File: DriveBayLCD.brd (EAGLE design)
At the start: 57.4 x 41.3 mm, 31 parts, among them J1 AVR_SPI_PRG_6PTH, U1 ATMEGA32U2-AU, U2 2N7002, X1 22-23-2041

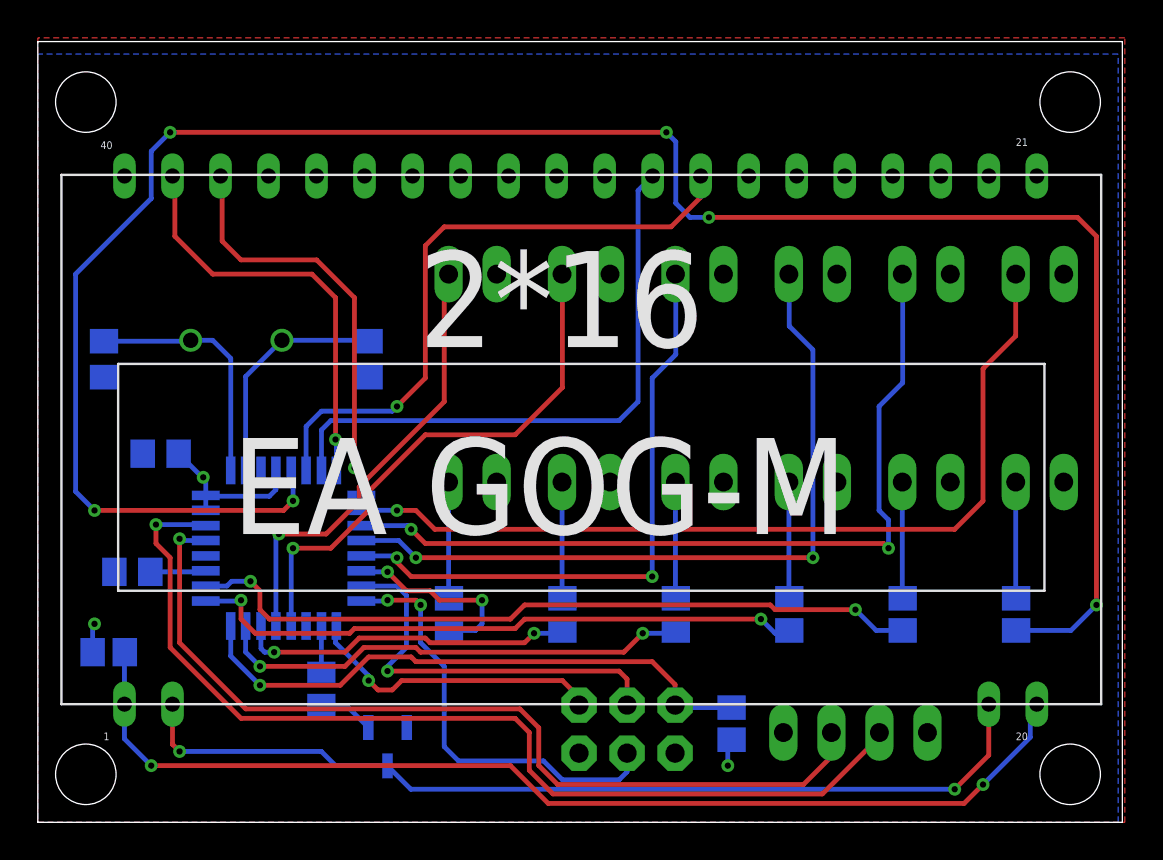
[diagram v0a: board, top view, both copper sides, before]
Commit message: Added mising 22 ohms line resistors
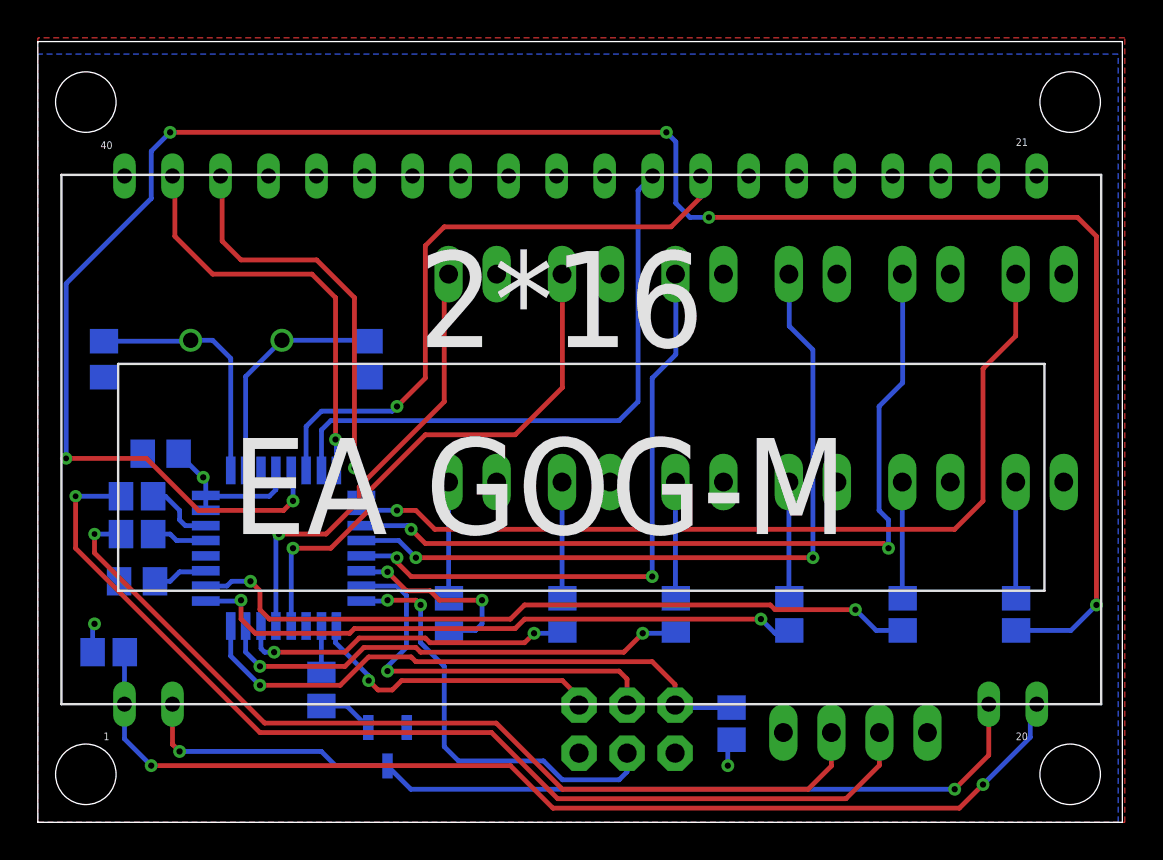
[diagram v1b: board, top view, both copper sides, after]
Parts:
- added R10, R11: 22, resistor:R0805
- moved C1 0.56 mm to (5.25, 12.8)
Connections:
- new net N$125: R10.1, U1.29
- new net N$126: R11.1, U1.30
- net D+: now also R10.2; no longer U1.29
- net D-: now also R11.2; no longer U1.30
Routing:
- net N$126: track 0.00 -> 3.72 mm
- net N$125: track 0.00 -> 2.93 mm
- net D-: track 52.9 -> 55.6 mm
- net D+: track 47.6 -> 48.8 mm
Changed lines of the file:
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@@
 <setting verticaltext="up"/>
 </settings>
-<grid distance="19.6850394" unitdist="mil" unit="mil" style="lines" multiple="1" display="no" altdistance="0.25" altunitdist="mm" altunit="mm"/>
+<grid distance="1" unitdist="mm" unit="mm" style="lines" multiple="1" display="no" altdistance="0.25" altunitdist="mm" altunit="mm"/>
 <layers>
-<layer number="1" name="Top" color="4" fill="1" visible="no" active="yes"/>
+<layer number="1" name="Top" color="4" fill="1" visible="yes" active="yes"/>
 <layer number="2" name="Route2" color="1" fill="3" visible="no" active="no"/>
 <layer number="3" name="Route3" color="4" fill="3" visible="no" active="no"/>
@@
 <attribute name="NAME" x="25.745" y="5.86" size="1.016" layer="26" rot="MR90"/>
 </element>
-<element name="C1" library="rcl" package="C0805" value="1µ" x="5" y="13.25" smashed="yes" rot="MR0">
-<attribute name="NAME" x="4.52" y="14.77" size="1.016" layer="26" rot="MR0"/>
+<element name="C1" library="rcl" package="C0805" value="1µ" x="5.25" y="12.75" smashed="yes" rot="MR0">
+<attribute name="NAME" x="4.77" y="14.27" size="1.016" layer="26" rot="MR0"/>
 </element>
 <element name="Q1" library="crystal" package="HC49/S" value="" x="10.5" y="25.5" smashed="yes" rot="MR180">
@@
 <attribute name="NAME" x="12.516" y="4.488" size="1.27" layer="26" rot="MR90"/>
 </element>
+<element name="R10" library="resistor" package="R0805" value="22" x="5.25" y="15.25" rot="MR0"/>
+<element name="R11" library="resistor" package="R0805" value="22" x="5.25" y="17.25" rot="MR0"/>
 </elements>
 <signals>
@@
 <signal name="D+">
 <contactref element="X1" pad="3"/>
-<contactref element="U1" pad="29"/>
-<wire x1="8.8852" y1="14.9064" x2="7.5936" y2="14.9064" width="0.254" layer="16"/>
-<wire x1="7.5936" y1="14.9064" x2="7.5" y2="15" width="0.254" layer="16"/>
-<via x="7.5" y="15" extent="1-16" drill="0.3302"/>
-<wire x1="7.5" y1="15" x2="7.5" y2="9.5" width="0.254" layer="1"/>
-<wire x1="7.5" y1="9.5" x2="11" y2="6" width="0.254" layer="1"/>
-<wire x1="11" y1="6" x2="25.5" y2="6" width="0.254" layer="1"/>
-<wire x1="25.5" y1="6" x2="26.5" y2="5" width="0.254" layer="1"/>
-<wire x1="26.5" y1="5" x2="26.5" y2="3" width="0.254" layer="1"/>
-<wire x1="26.5" y1="3" x2="27.5" y2="2" width="0.254" layer="1"/>
-<wire x1="27.5" y1="2" x2="40.5" y2="2" width="0.254" layer="1"/>
-<wire x1="40.5" y1="2" x2="42" y2="3.5" width="0.254" layer="1"/>
-<wire x1="42" y1="3.5" x2="42" y2="4.73" width="0.254" layer="1"/>
-<wire x1="42" y1="4.73" x2="41.98" y2="4.75" width="0.254" layer="1"/>
+<contactref element="R10" pad="2"/>
+<wire x1="41.98" y1="4.75" x2="41.98" y2="2.98" width="0.254" layer="1"/>
+<wire x1="41.98" y1="2.98" x2="40.75" y2="1.75" width="0.254" layer="1"/>
+<wire x1="40.75" y1="1.75" x2="27.75" y2="1.75" width="0.254" layer="1"/>
+<wire x1="27.75" y1="1.75" x2="24.25" y2="5.25" width="0.254" layer="1"/>
+<wire x1="24.25" y1="5.25" x2="12" y2="5.25" width="0.254" layer="1"/>
+<wire x1="4.4" y1="15.25" x2="3" y2="15.25" width="0.254" layer="16"/>
+<via x="3" y="15.25" extent="1-16" drill="0.3048"/>
+<wire x1="3" y1="15.25" x2="3" y2="14.25" width="0.254" layer="1"/>
+<wire x1="3" y1="14.25" x2="12" y2="5.25" width="0.254" layer="1"/>
 </signal>
 <signal name="D-">
 <contactref element="X1" pad="2"/>
-<contactref element="U1" pad="30"/>
-<wire x1="44.52" y1="4.75" x2="44.52" y2="4.52" width="0.254" layer="1"/>
-<wire x1="44.52" y1="4.52" x2="41.5" y2="1.5" width="0.254" layer="1"/>
-<wire x1="41.5" y1="1.5" x2="27.25" y2="1.5" width="0.254" layer="1"/>
-<wire x1="27.25" y1="1.5" x2="26" y2="2.75" width="0.254" layer="1"/>
-<wire x1="26" y1="2.75" x2="26" y2="4.75" width="0.254" layer="1"/>
-<wire x1="26" y1="4.75" x2="25.25" y2="5.5" width="0.254" layer="1"/>
-<wire x1="25.25" y1="5.5" x2="10.75" y2="5.5" width="0.254" layer="1"/>
-<wire x1="10.75" y1="5.5" x2="7" y2="9.25" width="0.254" layer="1"/>
-<wire x1="7" y1="9.25" x2="7" y2="14" width="0.254" layer="1"/>
-<wire x1="7" y1="14" x2="6.25" y2="14.75" width="0.254" layer="1"/>
-<wire x1="6.25" y1="14.75" x2="6.25" y2="15.75" width="0.254" layer="1"/>
-<via x="6.25" y="15.75" extent="1-16" drill="0.3302"/>
-<wire x1="6.25" y1="15.75" x2="8.829" y2="15.75" width="0.254" layer="16"/>
-<wire x1="8.829" y1="15.75" x2="8.8852" y2="15.6938" width="0.254" layer="16"/>
+<contactref element="R11" pad="2"/>
+<wire x1="4.4" y1="17.25" x2="2" y2="17.25" width="0.254" layer="16"/>
+<via x="2" y="17.25" extent="1-16" drill="0.3048"/>
+<wire x1="2" y1="17.25" x2="2" y2="14.5" width="0.254" layer="1"/>
+<wire x1="2" y1="14.5" x2="11.75" y2="4.75" width="0.254" layer="1"/>
+<wire x1="11.75" y1="4.75" x2="24" y2="4.75" width="0.254" layer="1"/>
+<wire x1="24" y1="4.75" x2="27.5" y2="1.25" width="0.254" layer="1"/>
+<wire x1="27.5" y1="1.25" x2="42.75" y2="1.25" width="0.254" layer="1"/>
+<wire x1="42.75" y1="1.25" x2="44.52" y2="3.02" width="0.254" layer="1"/>
+<wire x1="44.52" y1="4.75" x2="44.52" y2="3.02" width="0.254" layer="1"/>
 </signal>
 <signal name="XTAL1">
@@
 <via x="6" y="3" extent="1-16" drill="0.3302"/>
 <wire x1="6" y1="3" x2="25" y2="3" width="0.254" layer="1"/>
-<wire x1="25" y1="3" x2="27" y2="1" width="0.254" layer="1"/>
-<wire x1="27" y1="1" x2="49" y2="1" width="0.254" layer="1"/>
-<wire x1="49" y1="1" x2="50" y2="2" width="0.254" layer="1"/>
+<wire x1="25" y1="3" x2="27.25" y2="0.75" width="0.254" layer="1"/>
+<wire x1="27.25" y1="0.75" x2="48.75" y2="0.75" width="0.254" layer="1"/>
+<wire x1="48.75" y1="0.75" x2="50" y2="2" width="0.254" layer="1"/>
 <via x="50" y="2" extent="1-16" drill="0.3302"/>
 <wire x1="50" y1="2" x2="52.5" y2="4.5" width="0.254" layer="16"/>
@@
 <contactref element="U1" pad="27"/>
 <contactref element="C1" pad="1"/>
-<wire x1="5.95" y1="13.25" x2="8.829" y2="13.25" width="0.254" layer="16"/>
 <wire x1="8.829" y1="13.25" x2="8.8852" y2="13.3062" width="0.254" layer="16"/>
+<wire x1="8.829" y1="13.25" x2="7.5" y2="13.25" width="0.254" layer="16"/>
+<wire x1="7.5" y1="13.25" x2="7" y2="12.75" width="0.254" layer="16"/>
+<wire x1="7" y1="12.75" x2="6.2" y2="12.75" width="0.254" layer="16"/>
 </signal>
 <signal name="V$1">
@@
 <wire x1="55" y1="32" x2="35.5" y2="32" width="0.254" layer="1"/>
 <via x="35.5" y="32" extent="1-16" drill="0.3302"/>
-<wire x1="6" y1="33" x2="2" y2="29" width="0.254" layer="16"/>
-<wire x1="2" y1="29" x2="2" y2="17.5" width="0.254" layer="16"/>
-<wire x1="2" y1="17.5" x2="3" y2="16.5" width="0.254" layer="16"/>
-<via x="3" y="16.5" extent="1-16" drill="0.3302"/>
-<wire x1="3" y1="16.5" x2="13" y2="16.5" width="0.254" layer="1"/>
+<wire x1="6" y1="33" x2="1.5" y2="28.5" width="0.254" layer="16"/>
+<wire x1="1.5" y1="28.5" x2="1.5" y2="19.25" width="0.254" layer="16"/>
 <wire x1="13" y1="16.5" x2="13.5" y2="17" width="0.254" layer="1"/>
 <via x="13.5" y="17" extent="1-16" drill="0.3302"/>
@@
 <via x="33.25" y="36.5" extent="1-16" drill="0.3302"/>
 <via x="7" y="36.5" extent="1-16" drill="0.3302"/>
+<via x="1.5" y="19.25" extent="1-16" drill="0.3048"/>
+<wire x1="1.5" y1="19.25" x2="5.75" y2="19.25" width="0.254" layer="1"/>
+<wire x1="5.75" y1="19.25" x2="8.5" y2="16.5" width="0.254" layer="1"/>
+<wire x1="8.5" y1="16.5" x2="13" y2="16.5" width="0.254" layer="1"/>
 </signal>
 <signal name="LED2">
@@
 <wire x1="16.35" y1="6.15" x2="17.484" y2="5.016" width="0.254" layer="16"/>
 </signal>
+<signal name="N$126">
+<contactref element="U1" pad="30"/>
+<contactref element="R11" pad="1"/>
+<wire x1="8.8852" y1="15.6938" x2="7.8062" y2="15.6938" width="0.254" layer="16"/>
+<wire x1="7.8062" y1="15.6938" x2="7.5" y2="16" width="0.254" layer="16"/>
+<wire x1="7.5" y1="16" x2="7.5" y2="16.5" width="0.254" layer="16"/>
+<wire x1="7.5" y1="16.5" x2="6.75" y2="17.25" width="0.254" layer="16"/>
+<wire x1="6.75" y1="17.25" x2="6.1" y2="17.25" width="0.254" layer="16"/>
+</signal>
+<signal name="N$125">
+<contactref element="U1" pad="29"/>
+<contactref element="R10" pad="1"/>
+<wire x1="8.8852" y1="14.9064" x2="7.3436" y2="14.9064" width="0.254" layer="16"/>
+<wire x1="7.3436" y1="14.9064" x2="7" y2="15.25" width="0.254" layer="16"/>
+<wire x1="7" y1="15.25" x2="6.1" y2="15.25" width="0.254" layer="16"/>
+</signal>
 </signals>
